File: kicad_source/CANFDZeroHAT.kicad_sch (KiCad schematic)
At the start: 35 parts, among them CN1 RASPI-IO, CN2 XY2500R-F-3.81-4P, CN3 SM04B-GHS-TB, CN4 SM04B-GHS-TB, SW1 SS-3235S-L3, U1 MCP2518FDT-E/SL, U2 TCAN332GDR, Y1 X1E0000210808

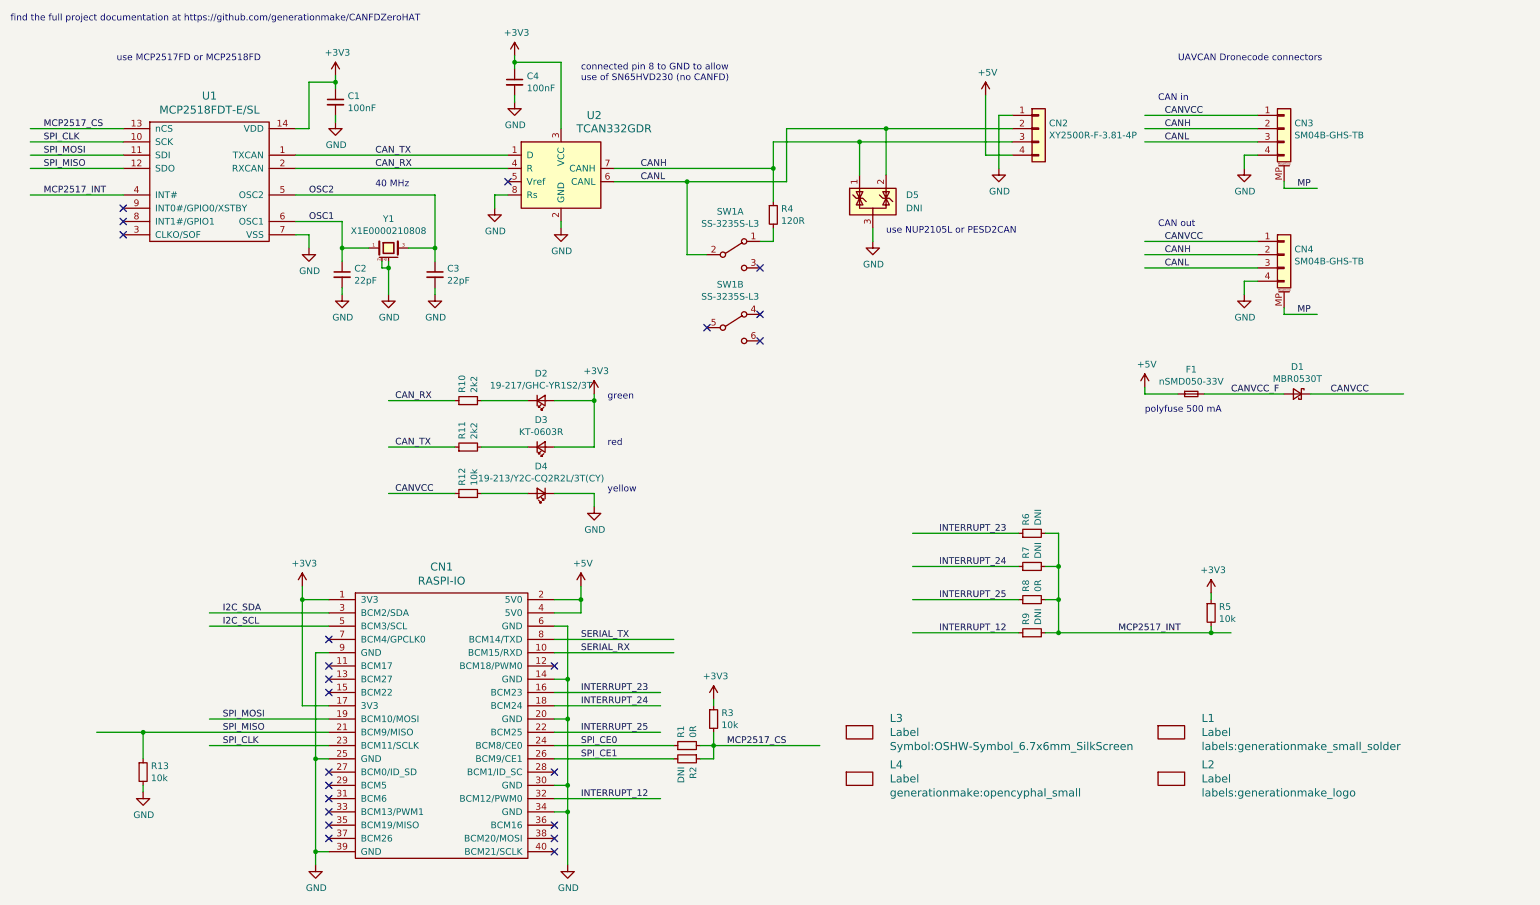
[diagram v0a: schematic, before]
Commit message: updated to KiCAD 8
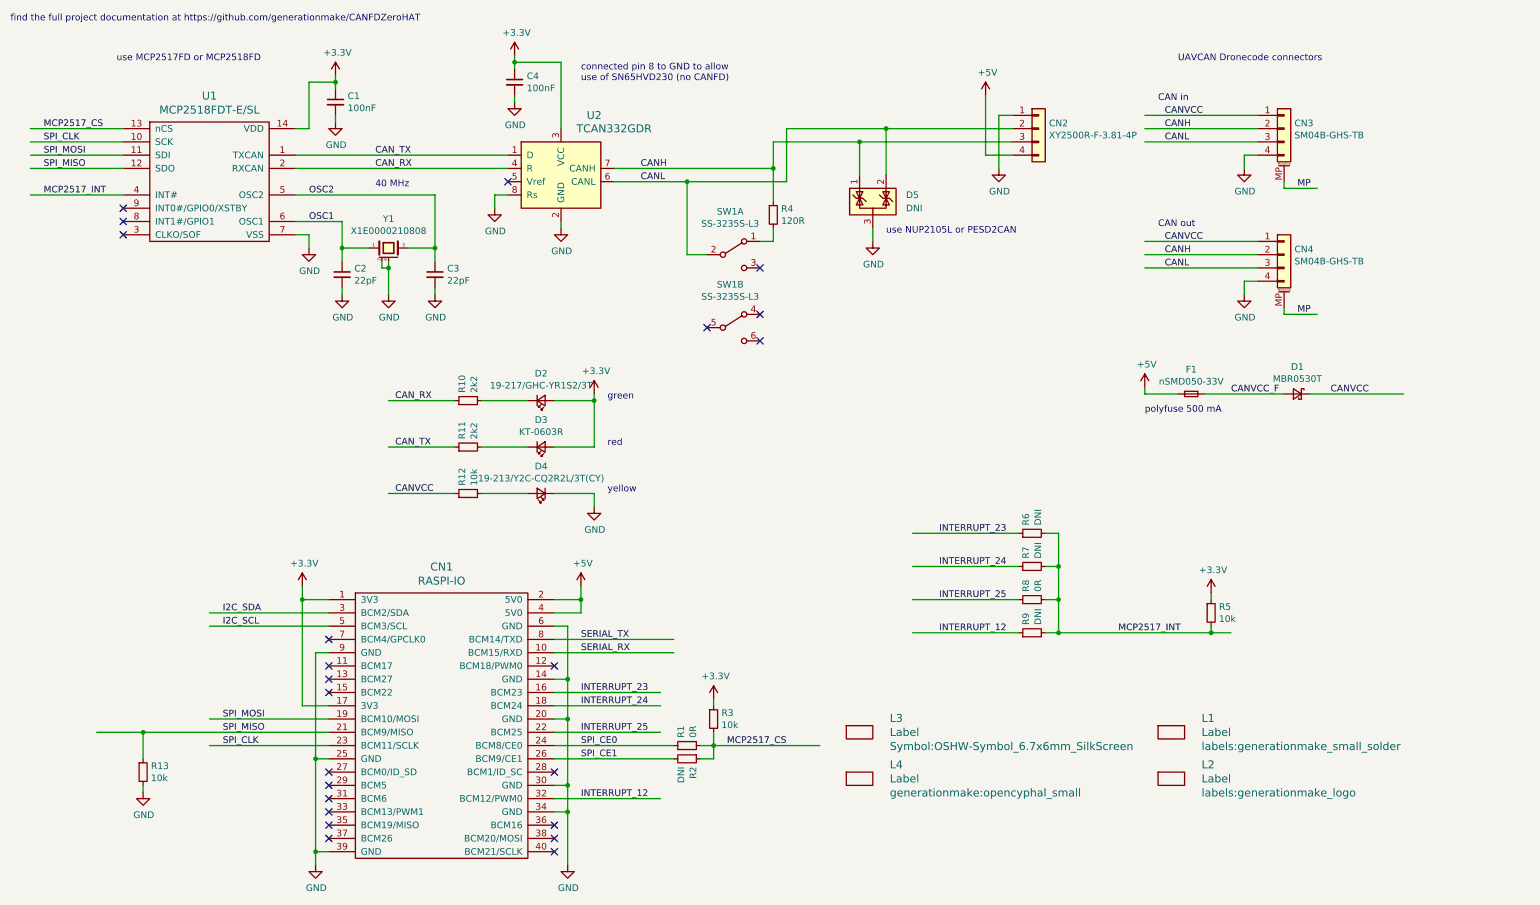
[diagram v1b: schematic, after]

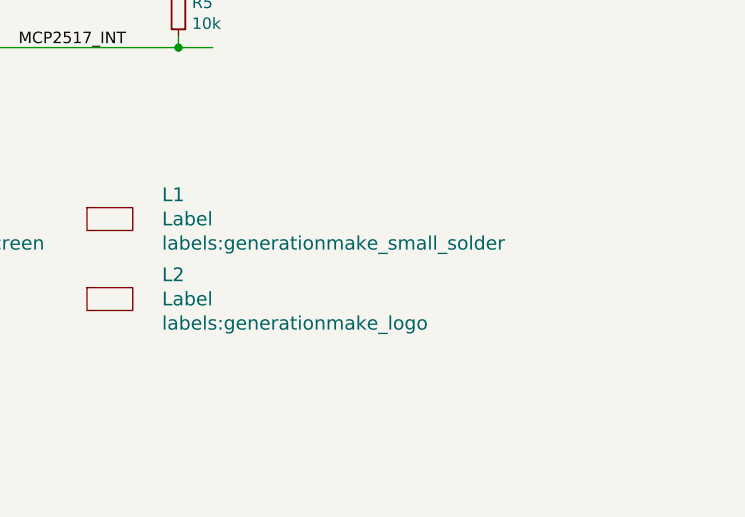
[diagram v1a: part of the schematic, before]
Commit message: fixed lirary errors and DRCs
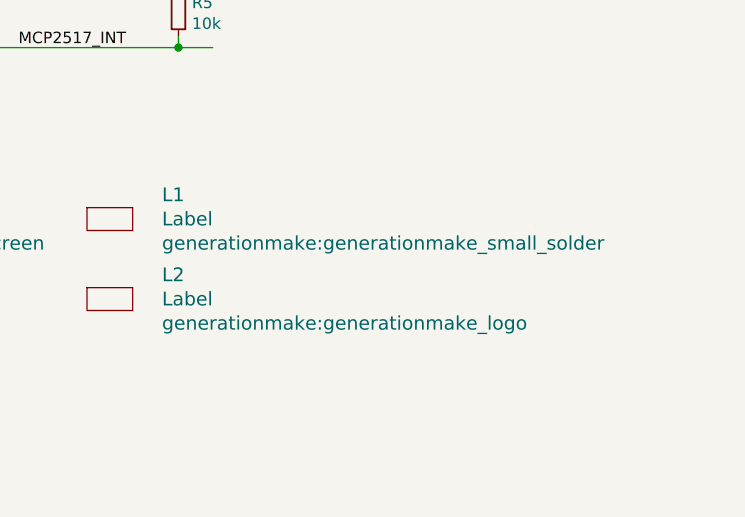
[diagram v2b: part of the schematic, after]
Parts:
- CN1: footprint MODULE_compute:RASPI_ZERO_HAT_EDGE -> generationmake:RASPI_ZERO_HAT_EDGE
- L1: footprint labels:generationmake_small_solder -> generationmake:generationmake_small_solder
- L2: footprint labels:generationmake_logo -> generationmake:generationmake_logo
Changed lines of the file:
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@@
 			)
 		)
-		(property "Footprint" "MODULE_compute:RASPI_ZERO_HAT_EDGE"
+		(property "Footprint" "generationmake:RASPI_ZERO_HAT_EDGE"
 			(at 92.71 125.73 0)
 			(effects
@@
 			)
 		)
-		(property "Footprint" "labels:generationmake_small_solder"
+		(property "Footprint" "generationmake:generationmake_small_solder"
 			(at 240.7412 153.8224 0)
 			(effects
@@
 			)
 		)
-		(property "Footprint" "labels:generationmake_logo"
+		(property "Footprint" "generationmake:generationmake_logo"
 			(at 240.7412 162.7124 0)
 			(effects
